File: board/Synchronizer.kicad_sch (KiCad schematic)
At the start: 46 parts, among them J1 Conn_01x02_Socket, J2 COIL1, J3 COIL2, Q1 2N3904, Q2 2N3906, Q3 IRF9540N, Q4 2N3904, U1 Pico, U2 LM7805_TO220, U3 LM358

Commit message: Added pcb2gcode generation of gcode for mill
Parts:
- R18: value 10k -> NC
- R5: value 1k -> 10k
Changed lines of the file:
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@@
       (effects (font (size 1.27 1.27)) (justify left))
     )
-    (property "Value" "10k" (at 138.43 132.08 90)
+    (property "Value" "NC" (at 138.43 132.08 90)
       (effects (font (size 1.27 1.27)) (justify left))
     )
@@
       (effects (font (size 1.27 1.27)) (justify left))
     )
-    (property "Value" "1k" (at 125.73 120.65 90)
-      (effects (font (size 1.27 1.27)) (justify left))
-    )
+    (property "Value" "10k" (at 125.73 120.65 90)
+      (effects (font (size 1.27 1.27)) (justify left))
+    )

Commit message: added extra gpio pins
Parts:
- removed J2: COIL1, MountingHole:MountingHole_2.2mm_M2_DIN965_Pad, symbol Connector:Conn_01x01_Pin
- removed J3: COIL2, MountingHole:MountingHole_2.2mm_M2_DIN965_Pad, symbol Connector:Conn_01x01_Pin
- added C11: 100 nF, Capacitor_THT:C_Disc_D5.0mm_W2.5mm_P5.00mm, symbol Device:C_Small
- added J2: Conn_01x14, Connector_PinHeader_2.54mm:PinHeader_1x14_P2.54mm_Vertical, symbol Connector_Generic:Conn_01x14
- added J4: Barrel_Jack_Switch, Connector_BarrelJack:BarrelJack_Horizontal, symbol Connector:Barrel_Jack_Switch
- added J5: COIL, TerminalBlock:TerminalBlock_bornier-2_P5.08mm, symbol Connector:Conn_01x02_Socket
- added R21: 10k, Resistor_THT:R_Axial_DIN0207_L6.3mm_D2.5mm_P7.62mm_Horizontal, symbol Device:R
- C10: footprint Capacitor_THT:CP_Radial_D12.5mm_P5.00mm -> Capacitor_THT:CP_Radial_D14.0mm_P5.00mm
- J1: value Conn_01x02_Socket -> POWER
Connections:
- net +12V: now also J4.1
- net AMPLITUDE: now also R21.1; no longer D3.1 (K)
- net GND: now also J2.12 (Pin_12), J2.2 (Pin_2), J2.7 (Pin_7), J4.2, J5.2 (Pin_2), R21.2
- net at C3.1, C4.1, C6.1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: now also J5.1 (Pin_1)
- net at R19.2: now also C11.1; no longer D4.2 (A)
- net at U1.10 (GPIO7): now also J2.4 (Pin_4)
- net at U1.11 (GPIO8): now also J2.5 (Pin_5)
- net at U1.12 (GPIO9): now also J2.6 (Pin_6)
- net at U1.14 (GPIO10): now also J2.8 (Pin_8)
- net at U1.15 (GPIO11): now also J2.9 (Pin_9)
- net at U1.16 (GPIO12): now also J2.10 (Pin_10)
- net at U1.17 (GPIO13): now also J2.11 (Pin_11)
- net at U1.19 (GPIO14): now also J2.13 (Pin_13)
- net at U1.20 (GPIO15): now also J2.14 (Pin_14)
- net at U1.7 (GPIO5): now also J2.1 (Pin_1)
- net at U1.9 (GPIO6): now also J2.3 (Pin_3)
- new net: C11.2, D3.1 (K), D4.2 (A)
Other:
- moved on the sheet: D4, R19

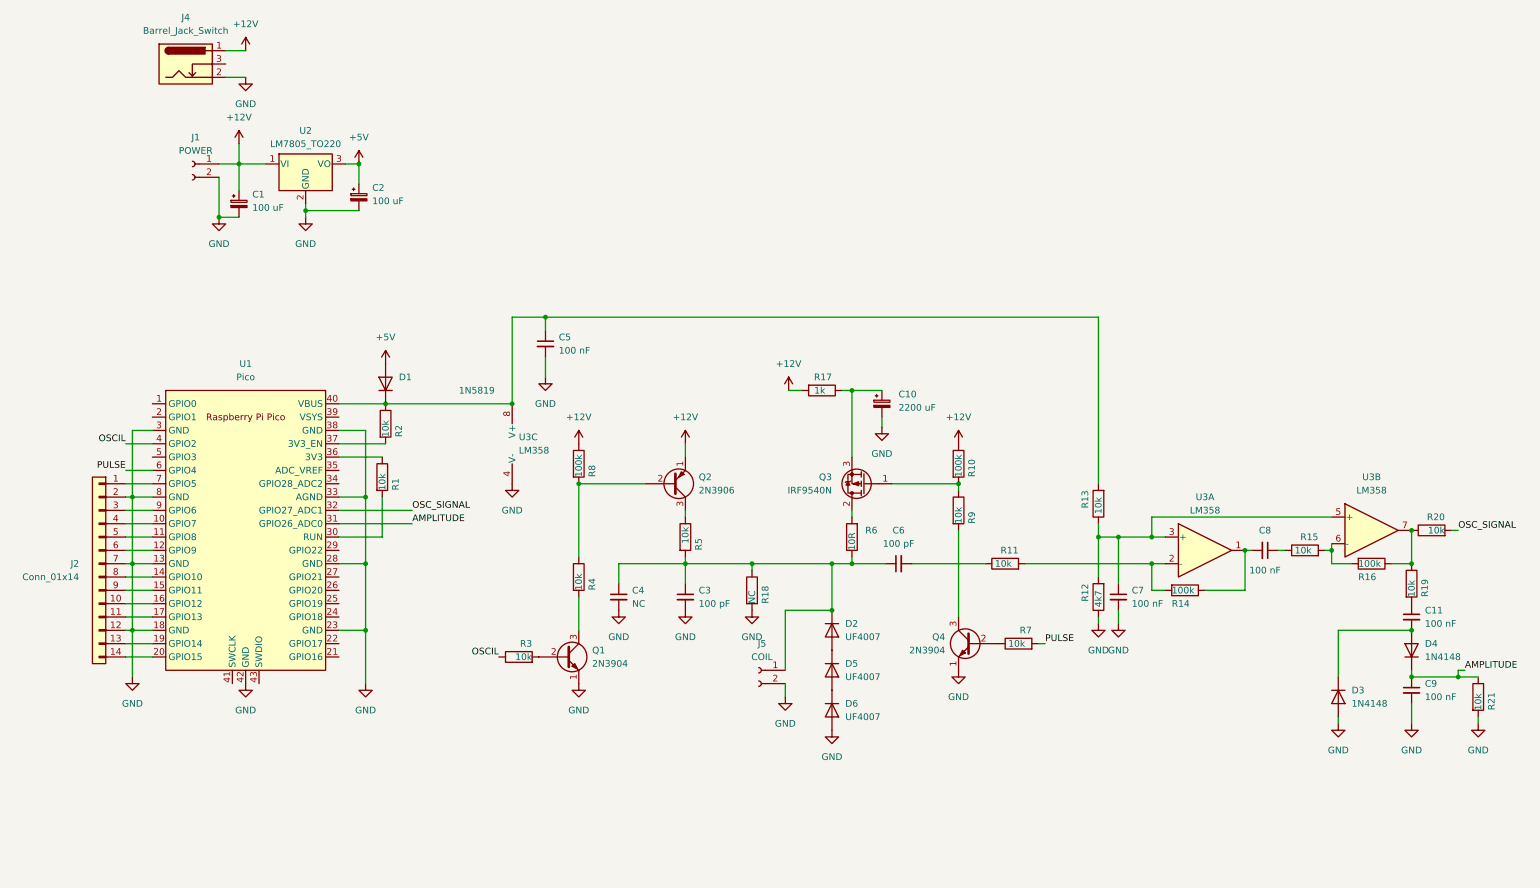
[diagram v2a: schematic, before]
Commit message: separate coils
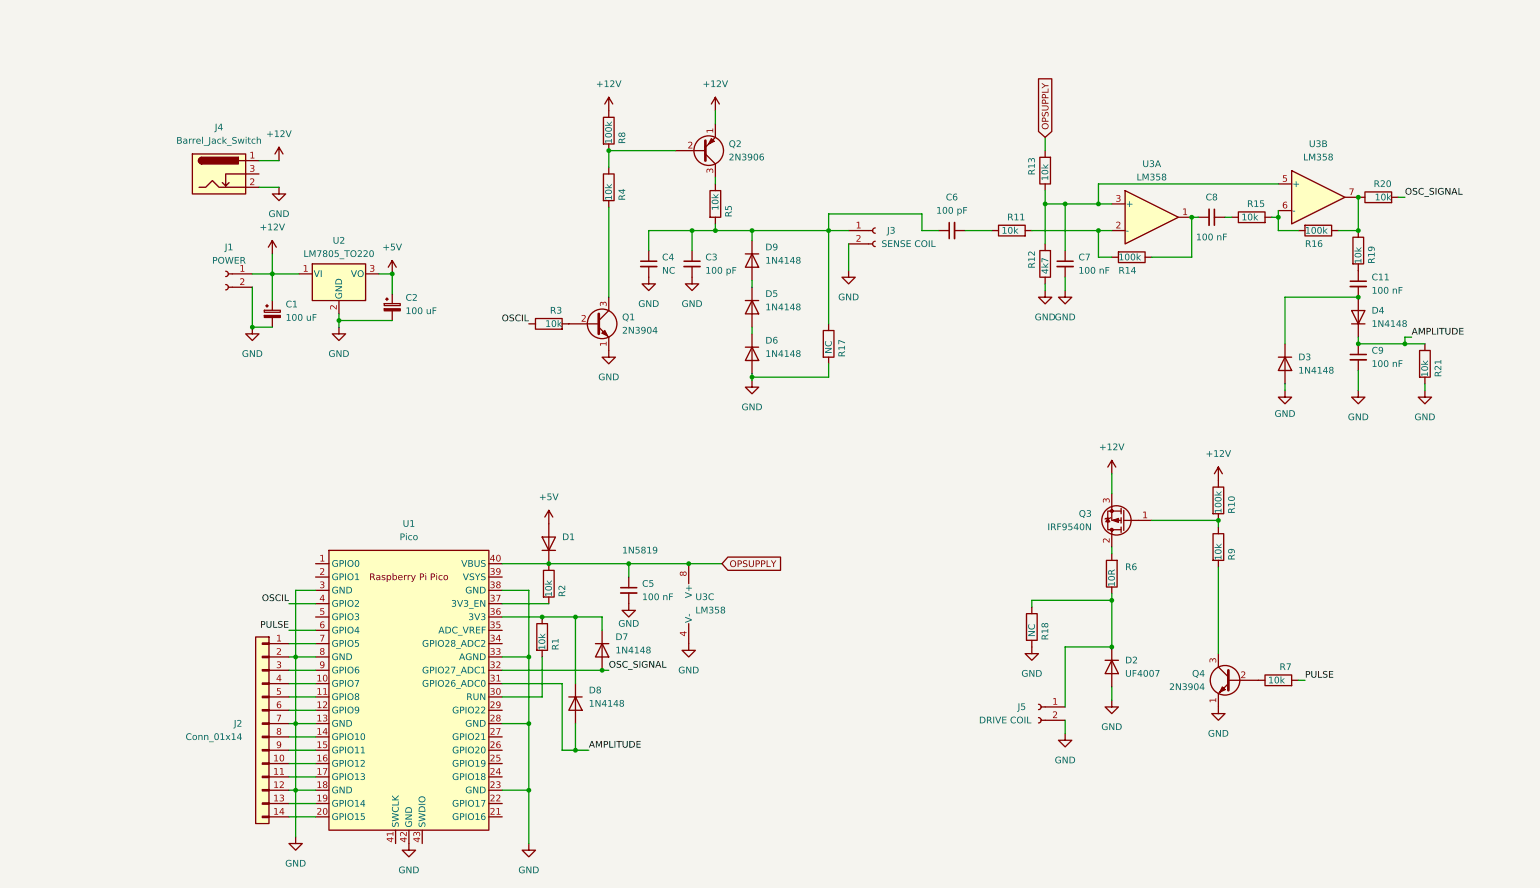
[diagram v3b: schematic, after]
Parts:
- removed C10: 2200 uF, Capacitor_THT:CP_Radial_D14.0mm_P5.00mm, symbol Device:C_Polarized_Small
- added D7, D8, D9: 1N4148, Diode_THT:D_DO-35_SOD27_P7.62mm_Horizontal, symbol Device:D
- added J3: SENSE COIL, TerminalBlock:TerminalBlock_bornier-2_P5.08mm, symbol Connector:Conn_01x02_Socket
- D5, D6: value UF4007 -> 1N4148; footprint Diode_THT:D_DO-41_SOD81_P7.62mm_Horizontal -> Diode_THT:D_DO-35_SOD27_P7.62mm_Horizontal
- J5: value COIL -> DRIVE COIL
- R17: value 1k -> NC; footprint Resistor_THT:R_Axial_DIN0614_L14.3mm_D5.7mm_P15.24mm_Horizontal -> Resistor_THT:R_Axial_DIN0207_L6.3mm_D2.5mm_P7.62mm_Horizontal
- R3: footprint Resistor_THT:R_Axial_DIN0207_L6.3mm_D2.5mm_P10.16mm_Horizontal -> Resistor_THT:R_Axial_DIN0207_L6.3mm_D2.5mm_P15.24mm_Horizontal
- R4, R9: footprint Resistor_THT:R_Axial_DIN0207_L6.3mm_D2.5mm_P10.16mm_Horizontal -> Resistor_THT:R_Axial_DIN0207_L6.3mm_D2.5mm_P7.62mm_Horizontal
- R7: footprint Resistor_THT:R_Axial_DIN0207_L6.3mm_D2.5mm_P7.62mm_Horizontal -> Resistor_THT:R_Axial_DIN0207_L6.3mm_D2.5mm_P15.24mm_Horizontal
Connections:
- net +12V: now also Q3.3 (S); no longer R17.2
- net AMPLITUDE: now also D8.2 (A)
- net GND: now also D2.2 (A), R17.2, J3.2 (Pin_2)
- net OSC_SIGNAL: now also D7.2 (A)
- net at R17.1: now also C3.1, C4.1, C6.1, R5.2, D9.1 (K), J3.1 (Pin_1); no longer Q3.3 (S)
- net OPSUPPLY: now reaches C5.1, D1.1 (K), R13.2, R2.1, U1.40 (VBUS), U3.8 (V+)
- net at D2.1 (K), J5.1 (Pin_1), R18.1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: no longer C3.1, C4.1, C6.1, R5.2
- net at R1.1, U1.36 (3V3): now also D7.1 (K), D8.1 (K)
- net at D5.1 (K): now also D9.2 (A); no longer D2.2 (A)
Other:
- moved on the sheet: C1, C11, C2, C3, C4, C5, C6, C7, C8, C9, D1, D2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
